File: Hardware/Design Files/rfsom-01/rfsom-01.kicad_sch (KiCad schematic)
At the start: 1 part

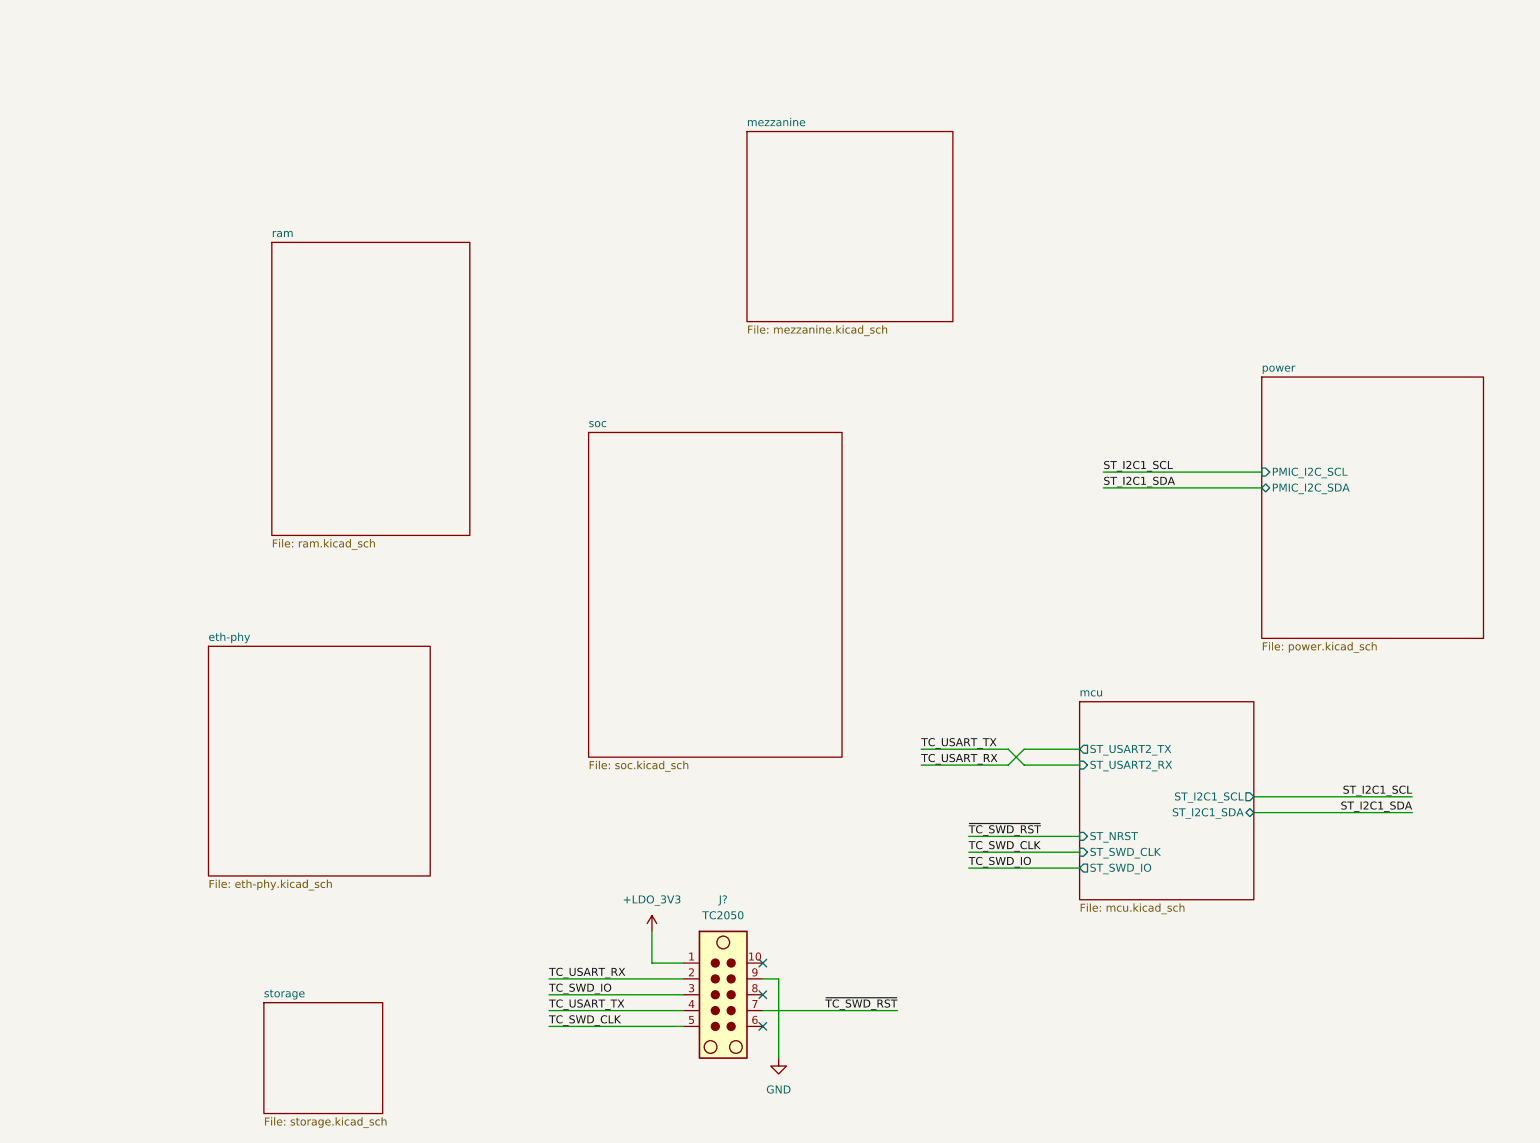
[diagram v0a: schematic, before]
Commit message: ddr progress; added more conns;
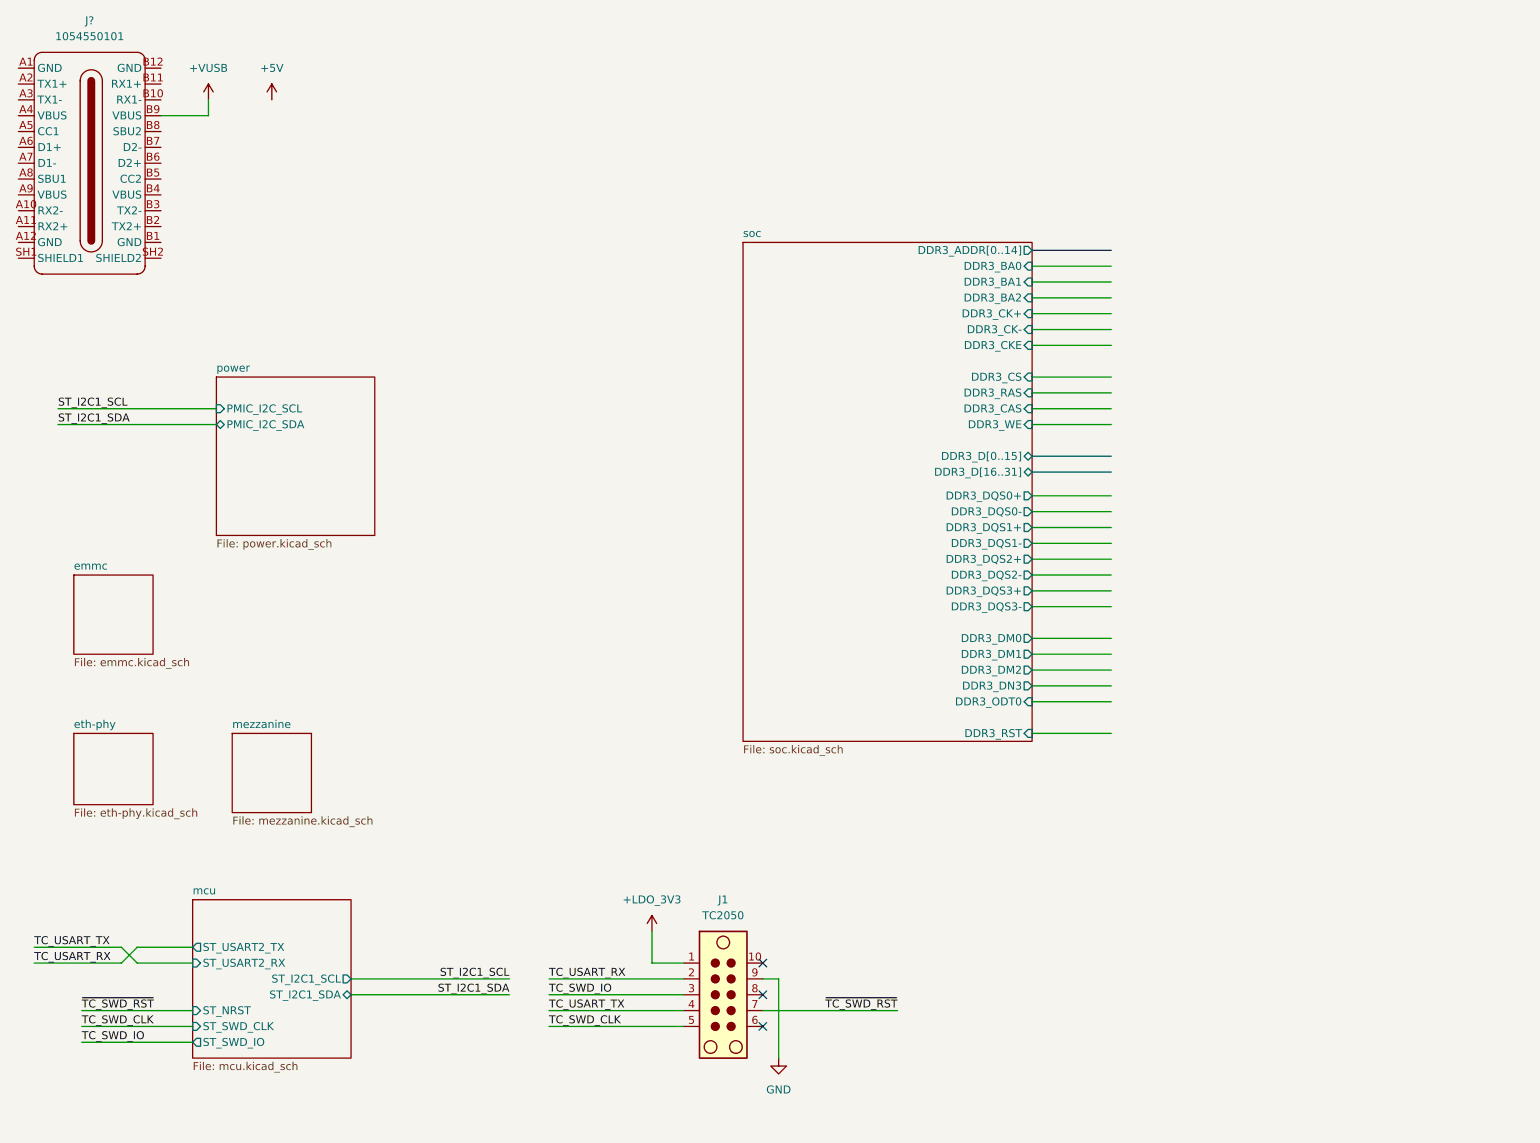
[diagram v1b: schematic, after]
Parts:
- added J?: 1054550101, Connectors:1054550101, symbol Connectors:1054550101
- gave numbers to parts that had none: 1
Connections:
- new net +VUSB: J?.B9 (VBUS)
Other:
- sheet storage renamed emmc
- removed sheet ram
- sheet emmc: file storage.kicad_sch -> emmc.kicad_sch
- sheet soc ports: added DDR3_ADDR[0..14], DDR3_BA0, DDR3_BA1, DDR3_BA2, DDR3_CAS, DDR3_CK+, DDR3_CK-, DDR3_CKE, DDR3_CS, DDR3_DM0, DDR3_DM1, DDR3_DM2, DDR3_DN3, DDR3_DQS0+, DDR3_DQS0-, DDR3_DQS1+, DDR3_DQS1-, DDR3_DQS2+, DDR3_DQS2-, DDR3_DQS3+, DDR3_DQS3-, DDR3_D[0..15], DDR3_D[16..31], DDR3_ODT0, DDR3_RAS, DDR3_RST, DDR3_WE; removed none

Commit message: ps progress; added ftdi; mezz pinout pedinging;
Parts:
- added FB?: MPZ1608S601ATA00, Resistor_SMD:R_0603_1608Metric, symbol Inductors:MPZ1608S601ATA00
- added R? (x2): RC0603FR-135K11L, Resistor_SMD:R_0603_1608Metric, symbol Resistors:RC0603FR-135K11L
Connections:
- net +VUSB: now also J?.A4 (VBUS), J?.A9 (VBUS), J?.B4 (VBUS), FB?.1
- net GND: now also J?.A1 (GND), J?.A12 (GND), J?.B1 (GND), J?.B12 (GND), J?.SH1 (SHIELD1), J?.SH2 (SHIELD2), R?.2, R?.2
- net at J?.A5 (CC1): now also R?.1
- net USBC_D+: now reaches J?.A6 (D1+)
- net USBC_D+: now also J?.B6 (D2+)
- net USBC_D-: now reaches J?.A7 (D1-)
- net USBC_D-: now also J?.B7 (D2-)
- net at J?.B5 (CC2): now also R?.1
- new net +VIN_5V0: FB?.2
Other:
- removed sheet emmc
- added sheet ftdi (ftdi.kicad_sch)
- sheet eth-phy ports: added ENET0_MDC, ENET0_RSTB, ENET0_RXCLK, ENET0_RXCTL, ENET0_RXD0, ENET0_RXD1, ENET0_RXD2, ENET0_RXD3, ENET0_TXCLK, ENET0_TXCTL, ENET0_TXD0, ENET0_TXD1, ENET0_TXD2, ENET0_TXD3, ETH0_MDIO, ETH_LED0, ETH_LED1, ETH_TXRXA+, ETH_TXRXA-, ETH_TXRXB+, ETH_TXRXB-, ETH_TXRXC+, ETH_TXRXC-, ETH_TXRXD+, ETH_TXRXD-, SYSCLK; removed none
- sheet soc ports: added none; removed DDR3_ADDR[0..14], DDR3_BA0, DDR3_BA1, DDR3_BA2, DDR3_CAS, DDR3_CK+, DDR3_CK-, DDR3_CKE, DDR3_CS, DDR3_DM0, DDR3_DM1, DDR3_DM2, DDR3_DN3, DDR3_DQS0+, DDR3_DQS0-, DDR3_DQS1+, DDR3_DQS1-, DDR3_DQS2+, DDR3_DQS2-, DDR3_DQS3+, DDR3_DQS3-, DDR3_D[0..15], DDR3_D[16..31], DDR3_ODT0, DDR3_RAS, DDR3_RST, DDR3_WE
- moved on the sheet: J?

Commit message: some ddr routing progress; layerstack per pcbway standard options, review reqd; commit prior to ddr split;
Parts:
- added H1, H2: MountingHole_Pad, MountingHole:MountingHole_2mm, symbol Mechanical:MountingHole_Pad
- gave numbers to parts that had none: 4
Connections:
- net GND: now also H1.1, H2.1
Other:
- sheet eth-phy ports: added ETH_LED2, ~{ENET0_RST}; removed ENET0_RSTB, ETH_LED0
- sheet mezzanine ports: added EXT_ETH_LED-ACT, EXT_ETH_LED-LINK, EXT_ETH_TRX0+, EXT_ETH_TRX0-, EXT_ETH_TRX1+, EXT_ETH_TRX1-, EXT_ETH_TRX2+, EXT_ETH_TRX2-, EXT_ETH_TRX3+, EXT_ETH_TRX3-; removed none
- sheet soc ports: added ENET0_MDC, ENET0_MDIO, ENET0_RXCLK, ENET0_RXCTL_R, ENET0_RXD0_R, ENET0_RXD1_R, ENET0_RXD2_R, ENET0_RXD3_R, ENET0_SYSCLK, ENET0_TXCLK_R, ENET0_TXCTL_R, ENET0_TXD0_R, ENET0_TXD1_R, ENET0_TXD2_R, ENET0_TXD3_R, EXT_SD_CD, EXT_SD_CLK, EXT_SD_CMD, EXT_SD_D0, EXT_SD_D1, EXT_SD_D2, EXT_SD_D3, EXT_VADC+, EXT_VADC-, JTAG_TCK_R, JTAG_TDI_R, JTAG_TDO_R, JTAG_TMS_R, USBH_OE, ~{ETH_RST}; removed none

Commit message: added starage, usb sch; more design progress in sch;
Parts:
- removed FB1: MPZ1608S601ATA00, Resistor_SMD:R_0603_1608Metric, symbol Inductors:MPZ1608S601ATA00
- removed J2: 1054550101, Connectors:1054550101, symbol Connectors:1054550101
- removed R6, R7: RC0603FR-135K11L, Resistor_SMD:R_0603_1608Metric, symbol Resistors:RC0603FR-135K11L
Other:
- sheet ftdi ports: added none; removed FTDI_USB_D+, FTDI_USB_D-
- moved on the sheet: J1
